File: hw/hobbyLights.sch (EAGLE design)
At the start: 48 parts, among them U1 MCP73831-2, U2 POWER, U3 BD48K28G, U4 ATMEGA32U4-AU, U5 TPS61222, Y1 RESONATORSMD

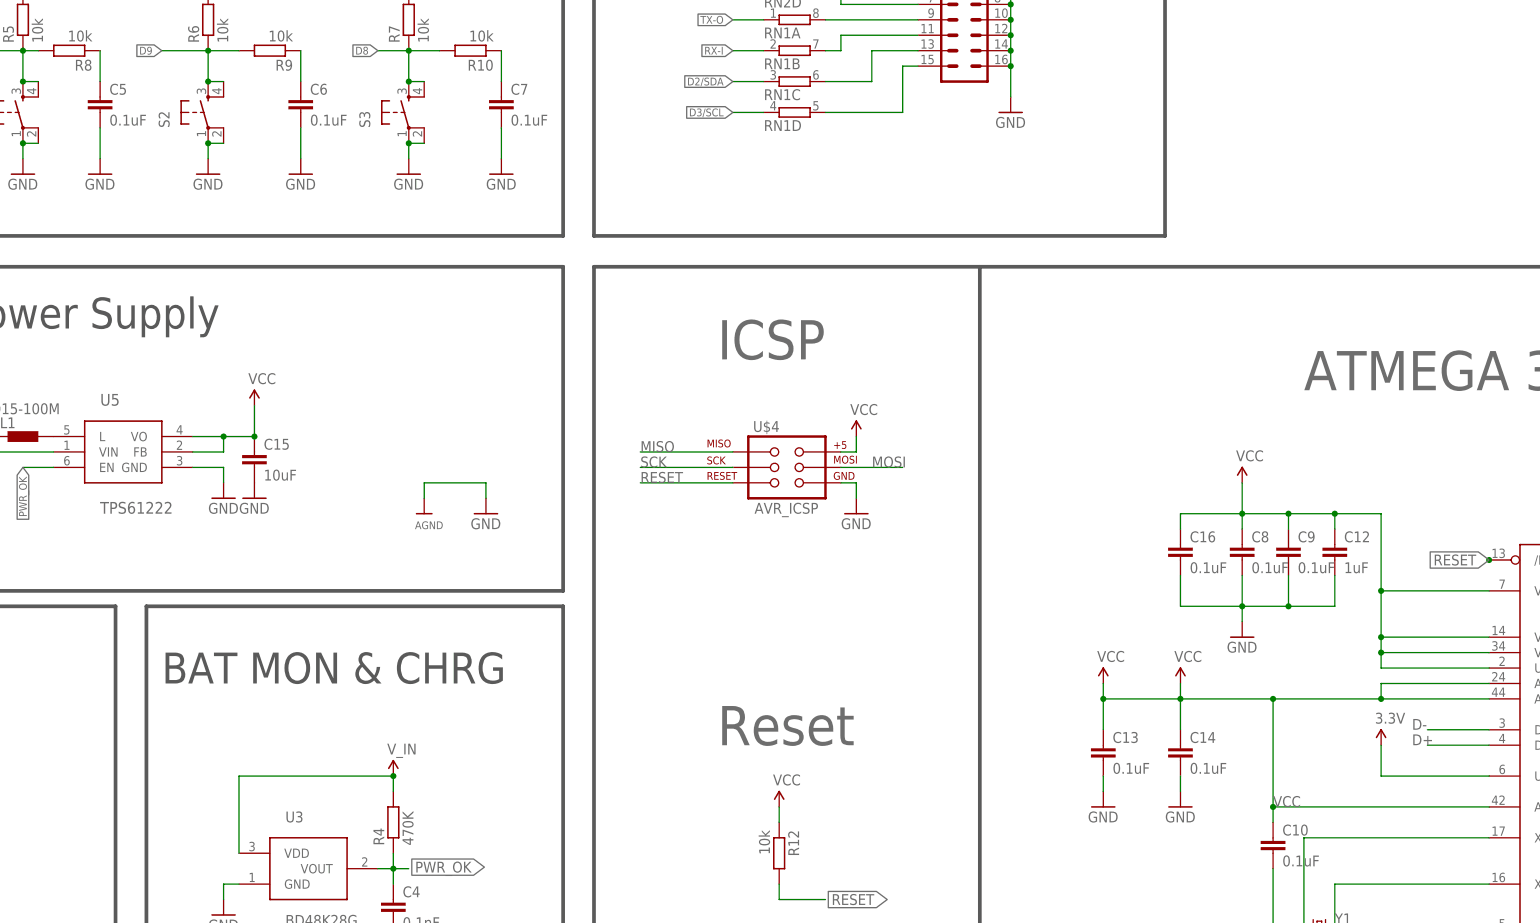
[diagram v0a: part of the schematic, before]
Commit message: Updated schematic for Rev B.
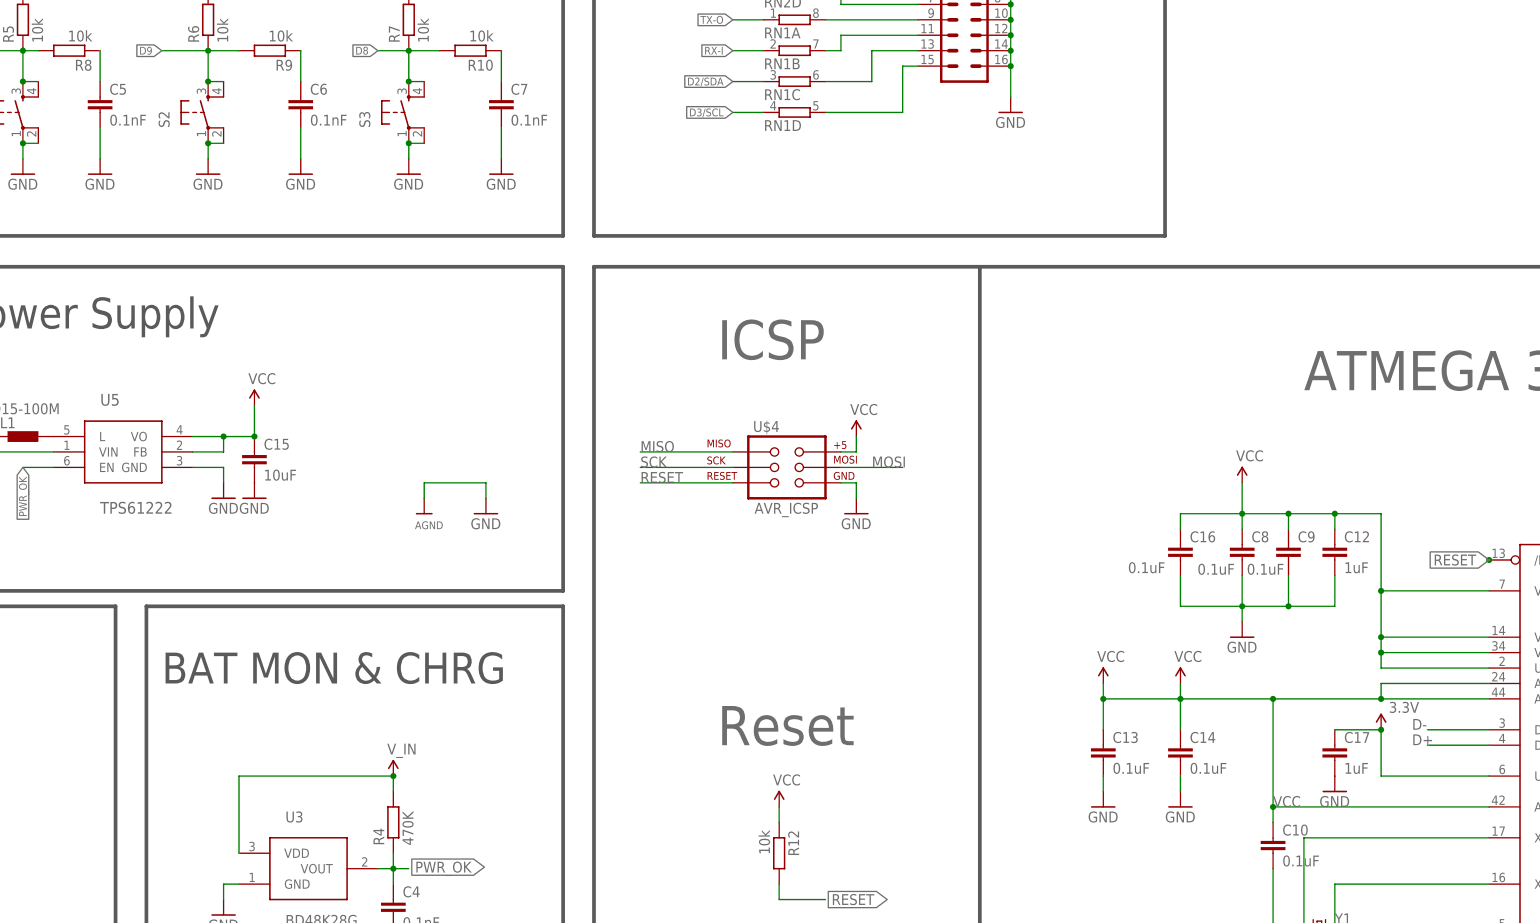
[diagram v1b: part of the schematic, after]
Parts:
- added C17: 1uF, rcl:C-EUC0603
- C5, C6, C7: value 0.1uF -> 0.1nF
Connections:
- net 3.3V: now also C17.1
- net GND: now also C17.2
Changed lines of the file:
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@@
 <?xml version="1.0" encoding="utf-8"?>
 <!DOCTYPE eagle SYSTEM "eagle.dtd">
-<eagle version="7.4.0">
+<eagle version="7.0.0">
 <drawing>
 <settings>
@@
 <part name="R9" library="rcl" deviceset="R-EU_" device="R0603" value="10k"/>
 <part name="R10" library="rcl" deviceset="R-EU_" device="R0603" value="10k"/>
-<part name="C5" library="rcl" deviceset="C-EU" device="C0603" value="0.1uF"/>
-<part name="C6" library="rcl" deviceset="C-EU" device="C0603" value="0.1uF"/>
-<part name="C7" library="rcl" deviceset="C-EU" device="C0603" value="0.1uF"/>
+<part name="C5" library="rcl" deviceset="C-EU" device="C0603" value="0.1nF"/>
+<part name="C6" library="rcl" deviceset="C-EU" device="C0603" value="0.1nF"/>
+<part name="C7" library="rcl" deviceset="C-EU" device="C0603" value="0.1nF"/>
 <part name="GND9" library="supply1" deviceset="GND" device=""/>
 <part name="GND10" library="supply1" deviceset="GND" device=""/>
@@
 <part name="VCC2" library="supply1" deviceset="VCCINT" device=""/>
 <part name="SUPPLY7" library="SparkFun-Aesthetics" deviceset="V_BATT" device="" value="V_IN"/>
+<part name="C17" library="rcl" deviceset="C-EU" device="C0603" value="1uF"/>
+<part name="GND16" library="SparkFun" deviceset="GND" device=""/>
 </parts>
 <sheets>
@@
 <instance part="GND18" gate="1" x="368.3" y="104.14" rot="MR0"/>
 <instance part="GND19" gate="1" x="287.02" y="53.34"/>
-<instance part="P+2" gate="G$1" x="284.48" y="104.14"/>
+<instance part="P+2" gate="G$1" x="284.48" y="106.68" smashed="yes">
+<attribute name="VALUE" x="285.75" y="109.474" size="1.778" layer="96"/>
+</instance>
 <instance part="Y1" gate="G$1" x="274.32" y="73.66"/>
 <instance part="GND22" gate="1" x="274.32" y="53.34"/>
@@
 <instance part="FRAME1" gate="G$2" x="287.02" y="0"/>
 <instance part="R11" gate="G$1" x="368.3" y="111.76" rot="R270"/>
-<instance part="C8" gate="G$1" x="261.62" y="137.16"/>
-<instance part="C9" gate="G$1" x="269.24" y="137.16"/>
+<instance part="C8" gate="G$1" x="261.62" y="137.16" smashed="yes">
+<attribute name="NAME" x="263.144" y="137.541" size="1.778" layer="95"/>
+<attribute name="VALUE" x="254.254" y="132.207" size="1.778" layer="96"/>
+</instance>
+<instance part="C9" gate="G$1" x="269.24" y="137.16" smashed="yes">
+<attribute name="NAME" x="270.764" y="137.541" size="1.778" layer="95"/>
+<attribute name="VALUE" x="262.382" y="132.207" size="1.778" layer="96"/>
+</instance>
 <instance part="C10" gate="G$1" x="266.7" y="88.9"/>
 <instance part="C12" gate="G$1" x="276.86" y="137.16"/>
@@
 <instance part="RN2" gate="C" x="187.96" y="233.68"/>
 <instance part="RN2" gate="D" x="187.96" y="228.6"/>
-<instance part="C16" gate="G$1" x="251.46" y="137.16"/>
+<instance part="C16" gate="G$1" x="251.46" y="137.16" smashed="yes">
+<attribute name="NAME" x="252.984" y="137.541" size="1.778" layer="95"/>
+<attribute name="VALUE" x="242.824" y="132.461" size="1.778" layer="96"/>
+</instance>
 <instance part="D1" gate="G$1" x="15.24" y="210.82" smashed="yes" rot="R90">
 <attribute name="NAME" x="13.462" y="212.1154" size="1.778" layer="95" rot="R180"/>
@@
 <instance part="VCC2" gate="G$1" x="96.52" y="30.48"/>
 <instance part="SUPPLY7" gate="G$1" x="121.92" y="99.06"/>
+<instance part="C17" gate="G$1" x="276.86" y="104.14"/>
+<instance part="GND16" gate="1" x="276.86" y="96.52"/>
 </instances>
 <busses>
@@
 <pinref part="C11" gate="G$1" pin="2"/>
 <pinref part="GND30" gate="1" pin="GND"/>
+</segment>
+<segment>
+<pinref part="C17" gate="G$1" pin="2"/>
+<pinref part="GND16" gate="1" pin="GND"/>
 </segment>
 </net>
@@
 <segment>
 <wire x1="284.48" y1="99.06" x2="302.26" y2="99.06" width="0.1524" layer="91"/>
-<wire x1="284.48" y1="99.06" x2="284.48" y2="104.14" width="0.1524" layer="91"/>
+<wire x1="284.48" y1="99.06" x2="284.48" y2="106.68" width="0.1524" layer="91"/>
 <pinref part="U4" gate="G$1" pin="UCAP"/>
 <pinref part="P+2" gate="G$1" pin="3.3V"/>
-</segment>
-</net>
+<pinref part="C17" gate="G$1" pin="1"/>
+<wire x1="284.48" y1="106.68" x2="276.86" y2="106.68" width="0.1524" layer="91"/>
+<junction x="284.48" y="106.68"/>
+</segment>
+</net>

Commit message: Updates for production - Rev B
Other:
- note added: "B"
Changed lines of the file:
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@@
 <wire x1="154.94" y1="182.88" x2="218.44" y2="182.88" width="0.6096" layer="97"/>
 <wire x1="218.44" y1="182.88" x2="218.44" y2="43.18" width="0.6096" layer="97"/>
+<text x="380.492" y="6.35" size="3.81" layer="95" ratio="12">B</text>
 </plain>
 <instances>

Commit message: Minor modifications and upgrade to Eagle 7.6.0
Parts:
- added U$12, U$13, U$14, U$15, U$16, U$17, U$18, U$19, U$20, U$21, U$22: NULL, fmc:NULL
- RN1, RN2: value (none) -> 470
- S1, S2, S3: value (none) -> microswitch
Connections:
- net A0: now also U$17.NC
- net A1: now also U$16.NC
- net A2: now also U$15.NC
- net A3: now also U$14.NC
- net A4: now also U$13.NC
- net A5: now also U$12.NC
- net D11: now also U$18.NC
- net D13: now also U$19.NC
- net D5: now also U$20.NC
- net D7: now also U$21.NC
- net RXLED: now also U$22.NC
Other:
- note added: "MCU Interface"
- note added: "MCU interface"
- note added: "Supply IF"
- note added: "USB battery charger and supply"

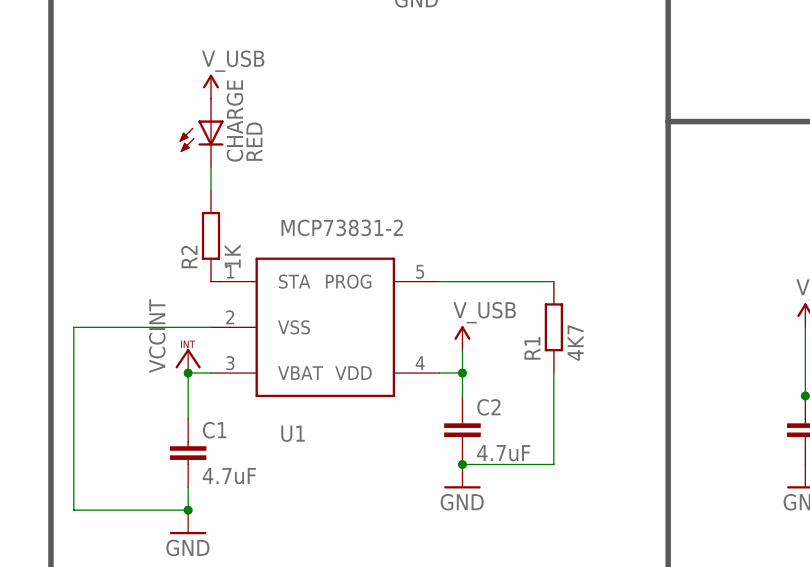
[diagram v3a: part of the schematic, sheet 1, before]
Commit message: HW: - updated resistor values to increase LED brightness. - updated resistor values to increase charge current. SW: - added new blink program - added new serial line command i.
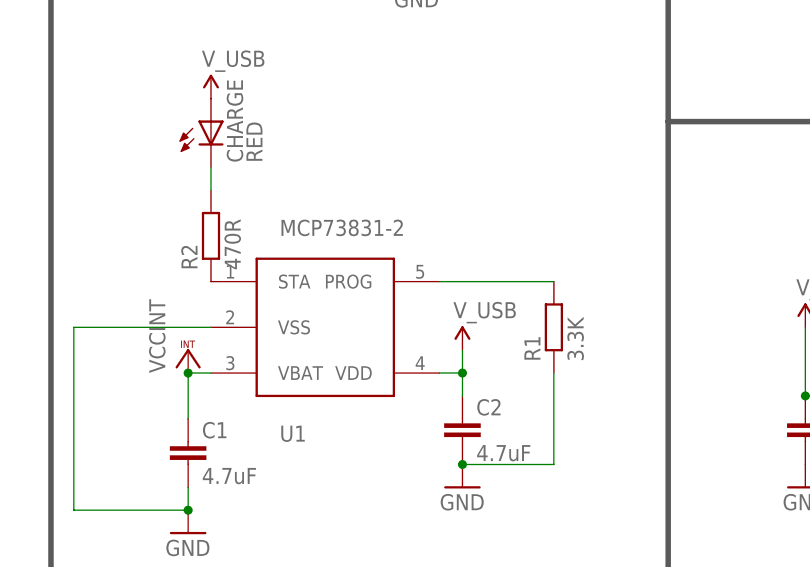
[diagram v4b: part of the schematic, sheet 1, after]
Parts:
- R1: value 4K7 -> 3.3K
- R2: value 1K -> 470R
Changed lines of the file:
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@@
 <parts>
 <part name="U1" library="fmc" deviceset="MCP73831-2" device=""/>
-<part name="R1" library="rcl" deviceset="R-EU_" device="R0603" value="4K7"/>
-<part name="R2" library="rcl" deviceset="R-EU_" device="R0603" value="1K"/>
+<part name="R1" library="rcl" deviceset="R-EU_" device="R0603" value="3.3K"/>
+<part name="R2" library="rcl" deviceset="R-EU_" device="R0603" value="470R"/>
 <part name="C1" library="rcl" deviceset="C-EU" device="C0805" value="4.7uF"/>
 <part name="C2" library="rcl" deviceset="C-EU" device="C0805" value="4.7uF"/>
